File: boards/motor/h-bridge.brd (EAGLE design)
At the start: 44.5 x 44.5 mm, 11 parts

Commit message: text change for V_batt resistors
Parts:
- BATT_H: value (none) -> 715k
- BATT_L: value (none) -> 165k
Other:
- board text added: "WolfBot Motor Board v2013.08.08"
- board text removed: "WolfBot Motor Board v2013.07.08"
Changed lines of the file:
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@@
 <dimension x1="3.058334375" y1="39.149025" x2="5.196665625" y2="41.495975" x3="-10.160003125" y3="53.339996875" textsize="1.778" layer="47" dtype="diameter" unit="inch" precision="3"/>
 <text x="28.6512" y="16.4846" size="0.8128" layer="22" font="vector" rot="MR0">En</text>
-<text x="28.2575" y="28.8925" size="1.016" layer="22" font="vector" rot="MR0">M3+</text>
-<text x="28.2575" y="26.3525" size="1.016" layer="22" font="vector" rot="MR0">M3-</text>
+<text x="33.8201" y="30.2895" size="1.016" layer="22" font="vector" rot="MR0">M3+</text>
+<text x="33.8201" y="27.7495" size="1.016" layer="22" font="vector" rot="MR0">M3-</text>
 <text x="28.5496" y="14.6304" size="0.8128" layer="22" font="vector" rot="MR0">M1</text>
 <text x="28.6004" y="12.7" size="0.8128" layer="22" font="vector" rot="MR0">D1</text>
@@
 <text x="36.5125" y="9.8425" size="1.778" layer="21" font="vector">BAT</text>
 <text x="36.5125" y="29.845" size="1.778" layer="21" font="vector">OUT</text>
-<text x="28.2575" y="36.5125" size="1.016" layer="22" font="vector" rot="MR0">M1-</text>
-<text x="28.2575" y="33.9725" size="1.016" layer="22" font="vector" rot="MR0">M2+</text>
-<text x="28.2575" y="31.4325" size="1.016" layer="22" font="vector" rot="MR0">M2-</text>
-<text x="28.2575" y="39.0525" size="1.016" layer="22" font="vector" rot="MR0">M1+</text>
+<text x="33.8201" y="37.9095" size="1.016" layer="22" font="vector" rot="MR0">M1-</text>
+<text x="33.8201" y="35.3695" size="1.016" layer="22" font="vector" rot="MR0">M2+</text>
+<text x="33.8201" y="32.8295" size="1.016" layer="22" font="vector" rot="MR0">M2-</text>
+<text x="33.8201" y="40.4495" size="1.016" layer="22" font="vector" rot="MR0">M1+</text>
 <text x="14.7955" y="38.9255" size="1.27" layer="21" font="vector">H1</text>
 <text x="11.3665" y="1.0795" size="1.27" layer="21" font="vector">H2</text>
 <text x="43.942" y="1.9939" size="1.016" layer="21" font="vector" align="bottom-right">WolfBot
 Motor Board
-v2013.07.08</text>
+v2013.08.08</text>
 <text x="28.702" y="3.556" size="0.8128" layer="22" font="vector" rot="MR0">B_V</text>
 </plain>
@@
 <attribute name="VALUE" x="21.59" y="39.243" size="1.27" layer="27" ratio="10" rot="R270"/>
 </element>
-<element name="OUT" library="con-molex-micro-fit-3_0" package="43045-0206" value="" x="41.91" y="24.765" rot="R90"/>
+<element name="OUT" library="con-molex-micro-fit-3_0" package="43045-0206" value="" x="41.91" y="24.765" smashed="yes" rot="R90"/>
 <element name="H2" library="st-microelectronics" package="DIL16" value="L293D" x="19.685" y="10.795" smashed="yes" rot="R270">
 <attribute name="OC_NEWARK" value="56P8249" x="-15.875" y="-13.335" size="1.778" layer="27" rot="R270" display="off"/>
@@
 </element>
 <element name="MOTORS" library="SparkFun-Connectors" package="1X06_LOCK" value="" x="29.845" y="40.005" smashed="yes" rot="MR270">
-<attribute name="NAME" x="32.385" y="29.845" size="1.27" layer="26" font="vector" rot="MR90"/>
 <attribute name="VALUE" x="33.147" y="41.275" size="1.27" layer="28" font="vector" rot="MR270"/>
 </element>
@@
 <element name="U$1" library="wolfbot" package="WSP1-T2-M6" value="ESWITCH-WSP1" x="2.54" y="29.21"/>
 <element name="R1" library="resistor" package="R0603" value="" x="15.494" y="42.164" rot="MR180"/>
-<element name="BATT_H" library="resistor" package="R0603" value="" x="35.306" y="22.6568" rot="MR0"/>
-<element name="BATT_L" library="resistor" package="R0603" value="" x="27.686" y="1.905" rot="MR0"/>
-<element name="U$3" library="jst-ph" package="JST-PH-SMD-90*" value="JST-PH8-SMD-90" x="39.0144" y="20.3708" rot="MR270"/>
+<element name="BATT_H" library="resistor" package="R0603" value="715k" x="35.306" y="22.6568" smashed="yes" rot="MR0">
+<attribute name="VALUE" x="36.2712" y="23.9268" size="0.8128" layer="28" rot="MR0"/>
+</element>
+<element name="BATT_L" library="resistor" package="R0603" value="165k" x="27.686" y="1.905" smashed="yes" rot="MR0">
+<attribute name="VALUE" x="30.2006" y="2.7178" size="0.8128" layer="28" rot="MR270"/>
+</element>
+<element name="U$3" library="jst-ph" package="JST-PH-SMD-90*" value="JST-PH8-SMD-90" x="39.0144" y="20.3708" smashed="yes" rot="MR270">
+<attribute name="VALUE" x="39.0144" y="-2.4892" size="1.27" layer="28" rot="MR0"/>
+</element>
 </elements>
 <signals>
@@
 <vertex x="48.26" y="48.26"/>
 </polygon>
-<polygon width="0.508" layer="16">
+<polygon width="0.508" layer="16" spacing="0.8128">
 <vertex x="-2.54" y="45.72"/>
 <vertex x="-2.54" y="-2.54"/>

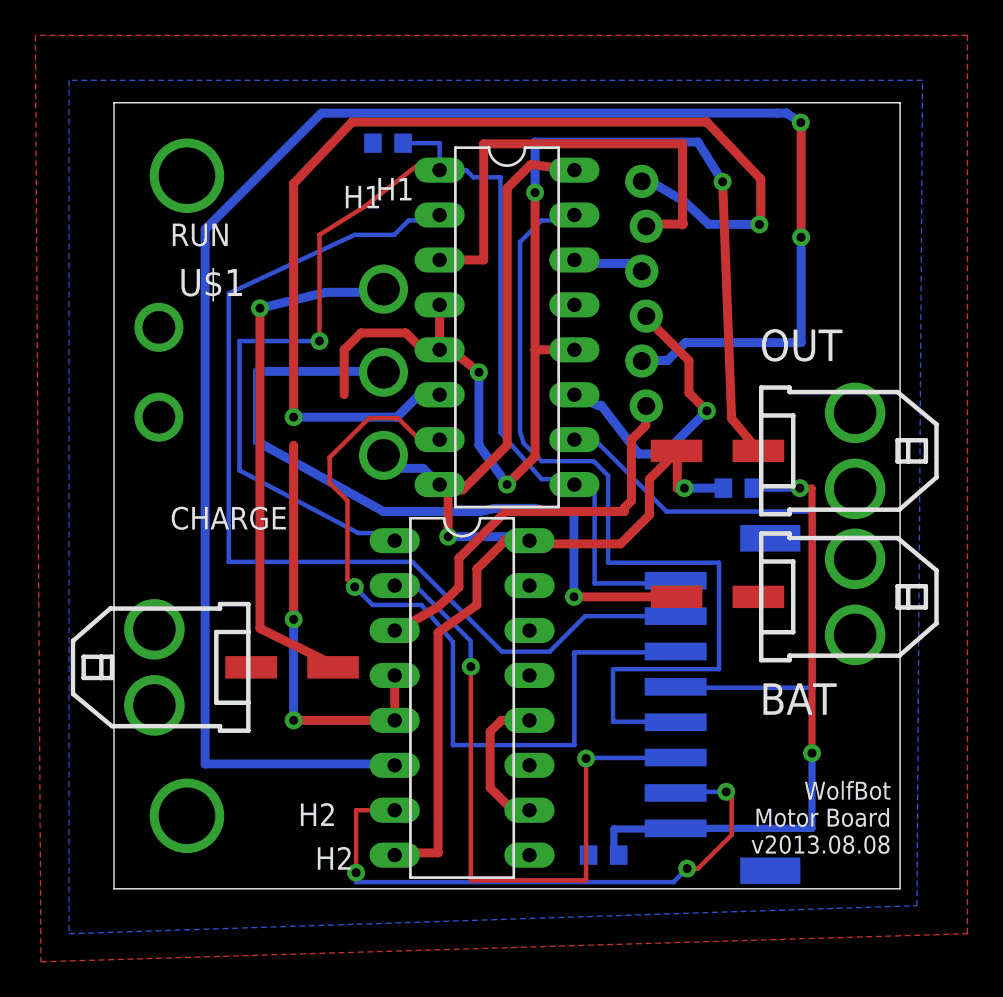
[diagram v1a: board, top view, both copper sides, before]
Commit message: Fix motor board silk screening
- add tValues and bValues to CAM job
- move resistor labels
- remove unwanted labels
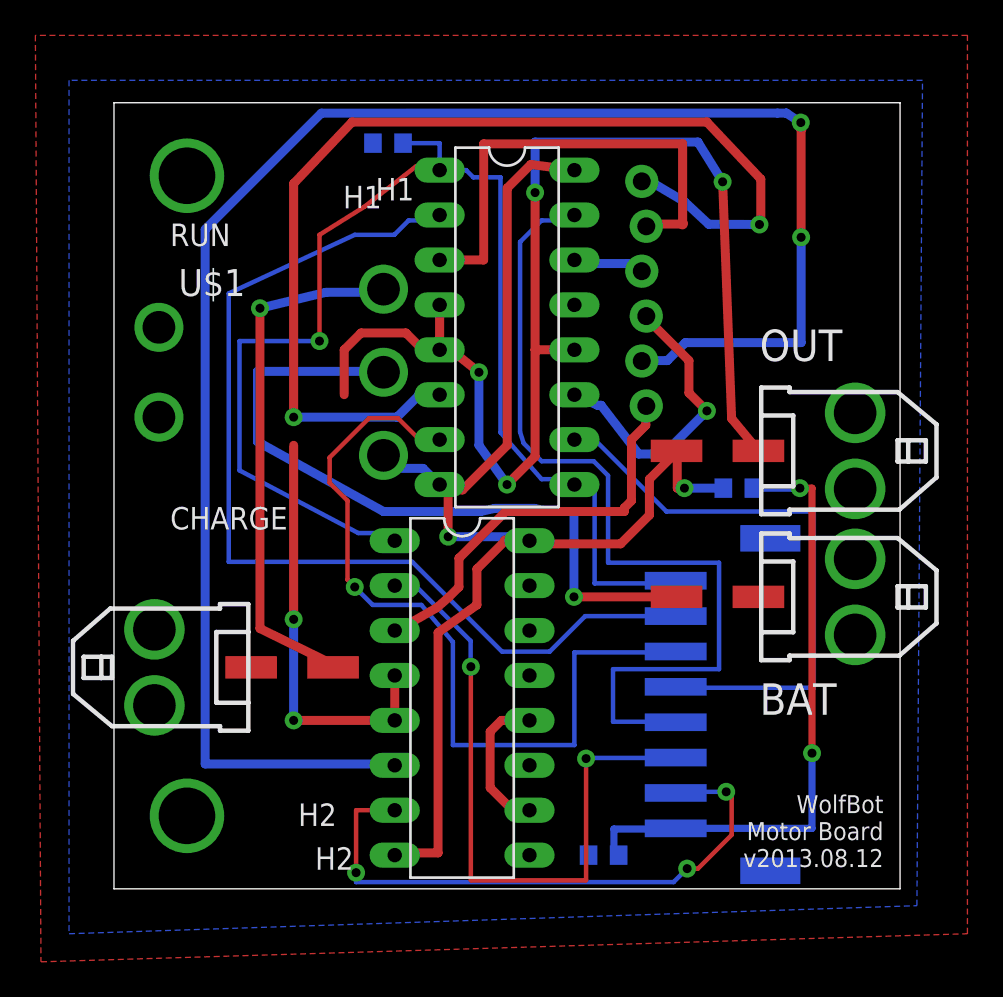
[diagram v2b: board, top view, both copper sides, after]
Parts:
- R1: value (none) -> 10k
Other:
- board text added: "WolfBot Motor Board v2013.08.12"
- board text removed: "WolfBot Motor Board v2013.08.08"
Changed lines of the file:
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@@
 <layer number="23" name="tOrigins" color="15" fill="1" visible="yes" active="yes"/>
 <layer number="24" name="bOrigins" color="15" fill="1" visible="yes" active="yes"/>
-<layer number="25" name="tNames" color="7" fill="1" visible="yes" active="yes"/>
-<layer number="26" name="bNames" color="7" fill="1" visible="yes" active="yes"/>
+<layer number="25" name="tNames" color="7" fill="1" visible="no" active="yes"/>
+<layer number="26" name="bNames" color="7" fill="1" visible="no" active="yes"/>
 <layer number="27" name="tValues" color="7" fill="1" visible="yes" active="yes"/>
 <layer number="28" name="bValues" color="7" fill="1" visible="yes" active="yes"/>
@@
 <text x="14.7955" y="38.9255" size="1.27" layer="21" font="vector">H1</text>
 <text x="11.3665" y="1.0795" size="1.27" layer="21" font="vector">H2</text>
-<text x="43.942" y="1.9939" size="1.016" layer="21" font="vector" align="bottom-right">WolfBot
+<text x="43.5102" y="1.2319" size="1.016" layer="21" font="vector" align="bottom-right">WolfBot
 Motor Board
-v2013.08.08</text>
+v2013.08.12</text>
 <text x="28.702" y="3.556" size="0.8128" layer="22" font="vector" rot="MR0">B_V</text>
 </plain>
@@
 <attribute name="OC_FARNELL" value="9589619" x="-0.635" y="7.62" size="1.778" layer="27" rot="R270" display="off"/>
 <attribute name="NAME" x="12.954" y="38.481" size="1.27" layer="25" ratio="10"/>
-<attribute name="VALUE" x="21.59" y="39.243" size="1.27" layer="27" ratio="10" rot="R270"/>
+<attribute name="VALUE" x="21.59" y="37.0078" size="1.27" layer="27" ratio="10" rot="R270"/>
 </element>
 <element name="OUT" library="con-molex-micro-fit-3_0" package="43045-0206" value="" x="41.91" y="24.765" smashed="yes" rot="R90"/>
@@
 <attribute name="OC_FARNELL" value="9589619" x="-15.875" y="-13.335" size="1.778" layer="27" rot="R270" display="off"/>
 <attribute name="NAME" x="10.414" y="3.556" size="1.27" layer="25" ratio="10"/>
-<attribute name="VALUE" x="19.05" y="18.288" size="1.27" layer="27" ratio="10" rot="R270"/>
+<attribute name="VALUE" x="19.05" y="9.0678" size="1.27" layer="27" ratio="10" rot="R270"/>
 </element>
 <element name="MOTORS" library="SparkFun-Connectors" package="1X06_LOCK" value="" x="29.845" y="40.005" smashed="yes" rot="MR270">
@@
 <element name="BAT" library="con-molex-micro-fit-3_0" package="43045-0206" value="" x="41.91" y="16.51" rot="R90"/>
 <element name="CHARGE" library="con-molex-micro-fit-3_0" package="43045-0206" value="" x="2.286" y="12.5222" rot="R270"/>
-<element name="U$1" library="wolfbot" package="WSP1-T2-M6" value="ESWITCH-WSP1" x="2.54" y="29.21"/>
-<element name="R1" library="resistor" package="R0603" value="" x="15.494" y="42.164" rot="MR180"/>
+<element name="U$1" library="wolfbot" package="WSP1-T2-M6" value="ESWITCH-WSP1" x="2.54" y="29.21" smashed="yes">
+<attribute name="NAME" x="3.65" y="33.52" size="1.524" layer="25" ratio="10"/>
+</element>
+<element name="R1" library="resistor" package="R0603" value="10k" x="15.494" y="42.164" smashed="yes" rot="MR180">
+<attribute name="VALUE" x="12.0904" y="42.4434" size="0.8128" layer="28" rot="MR180"/>
+</element>
 <element name="BATT_H" library="resistor" package="R0603" value="715k" x="35.306" y="22.6568" smashed="yes" rot="MR0">
 <attribute name="VALUE" x="36.2712" y="23.9268" size="0.8128" layer="28" rot="MR0"/>
 </element>
 <element name="BATT_L" library="resistor" package="R0603" value="165k" x="27.686" y="1.905" smashed="yes" rot="MR0">
-<attribute name="VALUE" x="30.2006" y="2.7178" size="0.8128" layer="28" rot="MR270"/>
-</element>
-<element name="U$3" library="jst-ph" package="JST-PH-SMD-90*" value="JST-PH8-SMD-90" x="39.0144" y="20.3708" smashed="yes" rot="MR270">
-<attribute name="VALUE" x="39.0144" y="-2.4892" size="1.27" layer="28" rot="MR0"/>
-</element>
+<attribute name="VALUE" x="26.035" y="3.5814" size="0.8128" layer="28" rot="MR270"/>
+</element>
+<element name="U$3" library="jst-ph" package="JST-PH-SMD-90*" value="JST-PH8-SMD-90" x="39.0144" y="20.3708" smashed="yes" rot="MR270"/>
 </elements>
 <signals>

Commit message: Fixed pull down, and three res sizes
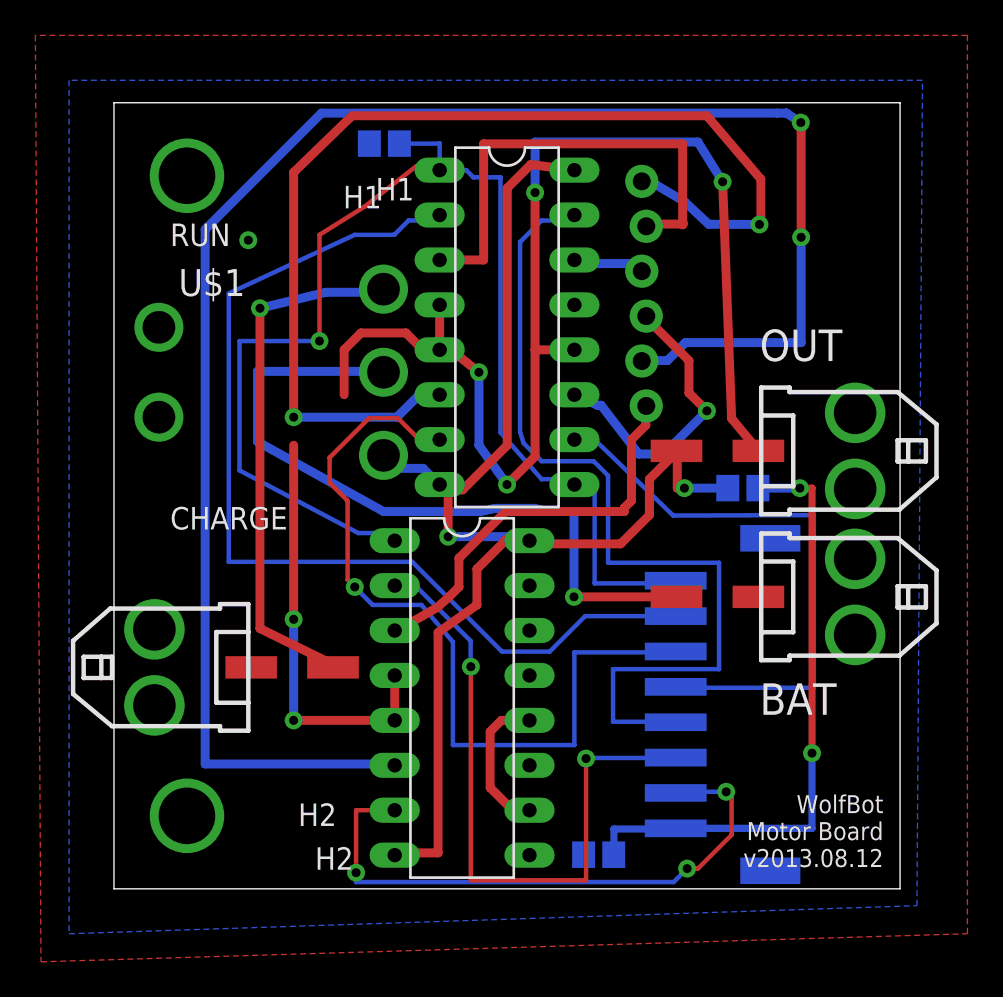
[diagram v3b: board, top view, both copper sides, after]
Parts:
- removed R1: 10k, resistor:R0603
- added EN_D: 10k, resistor:R0805
- BATT_H, BATT_L: device resistor:R0603 -> resistor:R0805
- moved BATT_L 0.28 mm to (27.4, 1.93), turned to 180 degrees
- moved BATT_H 0.25 mm to (35.6, 22.7)
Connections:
- net ENABLE: now also EN_D.2; no longer R1.2
- net GND: now also BATT_L.1, EN_D.1; no longer BATT_L.2, R1.1
- net N$2: now also BATT_L.2; no longer BATT_L.1
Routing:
- net M1+: track 61.4 -> 62.1 mm
- net M3_DIR: track 35.5 -> 36.1 mm
- net N$2: track 36.8 -> 36.3 mm
- net GND: vias 6 -> 7

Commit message: Cleanup issues, working on powerboard res move
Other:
- board text added: "WolfBot Motor Board v2013.09.26"
- board text removed: "WolfBot Motor Board v2013.08.12"
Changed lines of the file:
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@@
 <setting verticaltext="up"/>
 </settings>
-<grid distance="1" unitdist="mil" unit="mil" style="lines" multiple="10" display="yes" altdistance="0.0125" altunitdist="inch" altunit="inch"/>
+<grid distance="0.01" unitdist="mm" unit="mm" style="lines" multiple="10" display="yes" altdistance="0.0125" altunitdist="inch" altunit="inch"/>
 <layers>
 <layer number="1" name="Top" color="4" fill="1" visible="yes" active="yes"/>
@@
 <text x="43.5102" y="1.2319" size="1.016" layer="21" font="vector" align="bottom-right">WolfBot
 Motor Board
-v2013.08.12</text>
+v2013.09.26</text>
 <text x="28.702" y="3.556" size="0.8128" layer="22" font="vector" rot="MR0">B_V</text>
+<circle x="4.1275" y="40.3225" radius="3.668" width="0.4064" layer="21"/>
+<text x="4.495" y="36.3474" size="1.27" layer="22" font="vector" rot="MR0">RUN</text>
+<text x="3.175" y="20.32" size="1.27" layer="21" font="vector">CHARGE</text>
+<text x="7.735" y="20.26" size="1.27" layer="22" font="vector" rot="MR0">CHARGE</text>
+<circle x="4.1275" y="4.1275" radius="3.668" width="0.4064" layer="21"/>
 </plain>
 <attributes>

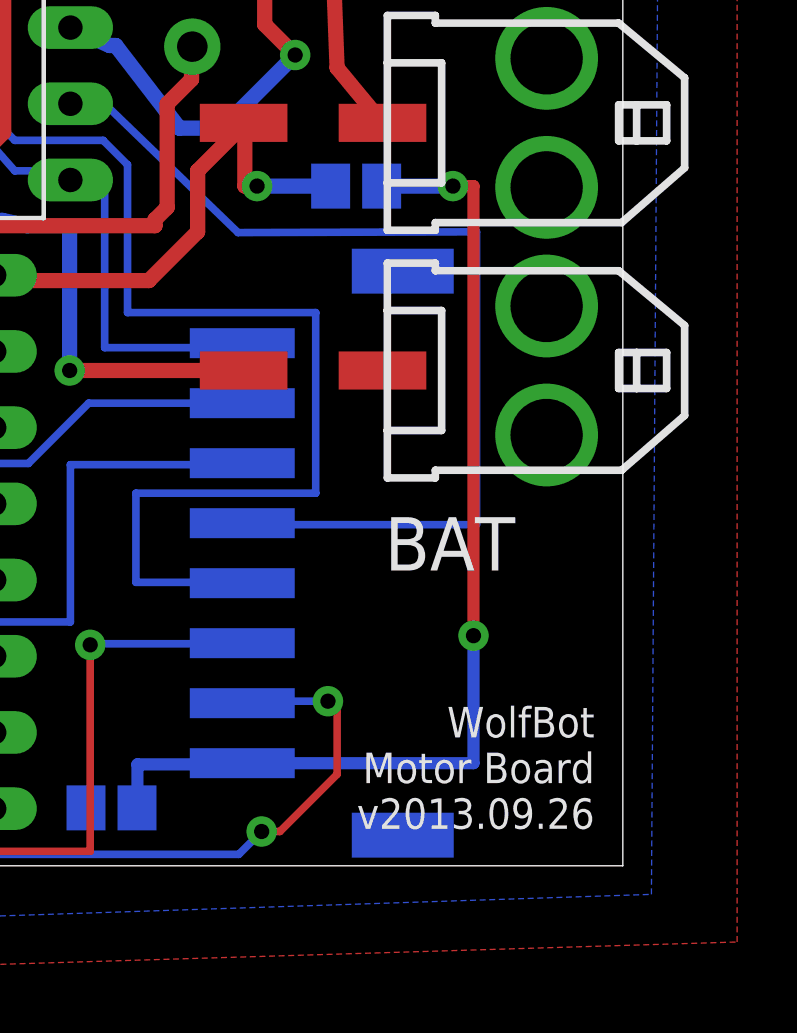
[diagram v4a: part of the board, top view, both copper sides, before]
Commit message: fixed via short problem
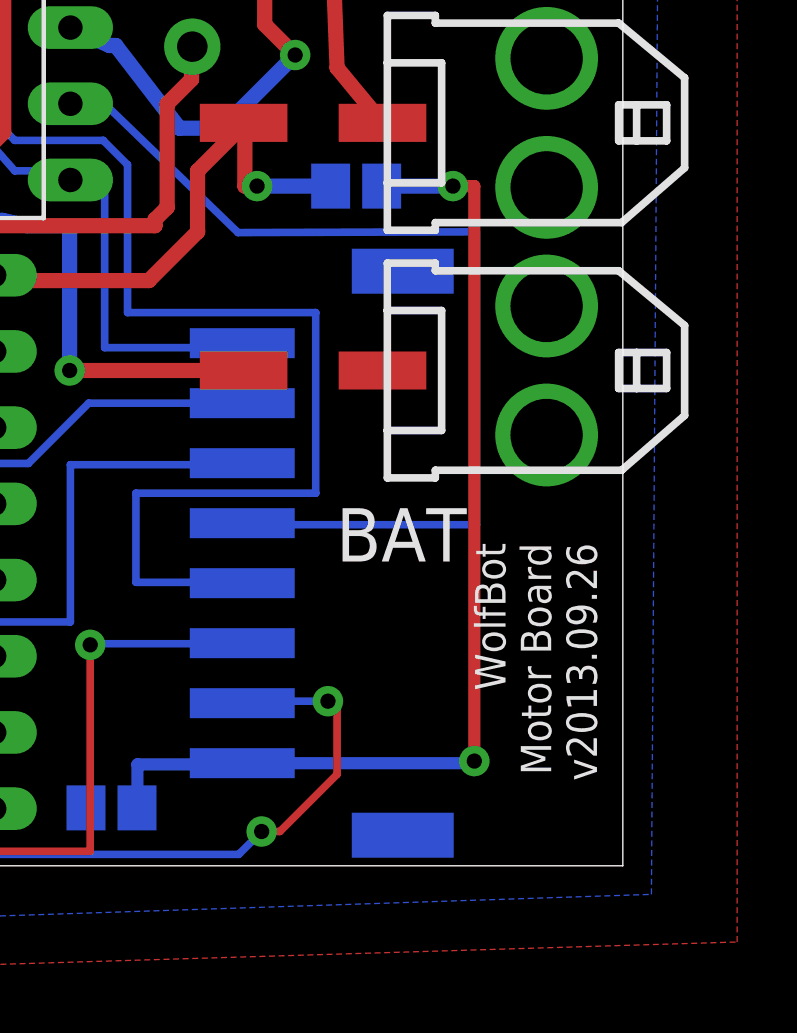
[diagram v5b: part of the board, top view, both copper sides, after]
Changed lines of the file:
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@@
 <text x="3.175" y="20.32" size="1.27" layer="21" font="vector">CHARGE</text>
 <text x="3.175" y="36.3474" size="1.27" layer="21" font="vector">RUN</text>
-<text x="36.5125" y="9.8425" size="1.778" layer="21" font="vector">BAT</text>
+<text x="34.8925" y="10.1425" size="1.778" layer="21" font="vector">BAT</text>
 <text x="36.5125" y="29.845" size="1.778" layer="21" font="vector">OUT</text>
 <text x="33.8201" y="37.9095" size="1.016" layer="22" font="vector" rot="MR0">M1-</text>
@@
 <text x="14.7955" y="38.9255" size="1.27" layer="21" font="vector">H1</text>
 <text x="11.3665" y="1.0795" size="1.27" layer="21" font="vector">H2</text>
-<text x="43.5102" y="1.2319" size="1.016" layer="21" font="vector" align="bottom-right">WolfBot
+<text x="43.5881" y="10.7602" size="1.016" layer="21" font="vector" rot="R90" align="bottom-right">WolfBot
 Motor Board
 v2013.09.26</text>
@@
 <wire x1="28.2702" y1="3.38125" x2="31.2535625" y2="3.38125" width="0.4064" layer="16"/>
 <via x="38.7858" y="22.6568" extent="1-16" drill="0.508" alwaysstop="yes"/>
-<wire x1="38.7858" y1="22.6568" x2="39.4716" y2="22.6568" width="0.4064" layer="1"/>
-<wire x1="39.4716" y1="22.6568" x2="39.4716" y2="7.6708" width="0.4064" layer="1"/>
-<via x="39.4716" y="7.6708" extent="1-16" drill="0.508" alwaysstop="yes"/>
-<wire x1="39.4716" y1="7.6708" x2="39.4716" y2="3.4208" width="0.4064" layer="16"/>
+<wire x1="38.7858" y1="22.6568" x2="39.5" y2="22.6568" width="0.4064" layer="1"/>
+<wire x1="39.5" y1="22.6568" x2="39.5" y2="3.4908" width="0.4064" layer="1"/>
+<via x="39.5" y="3.4908" extent="1-16" drill="0.508" alwaysstop="yes"/>
+<wire x1="39.5" y1="3.4908" x2="39.4716" y2="3.4208" width="0.4064" layer="16"/>
 <wire x1="39.4716" y1="3.4208" x2="31.7644" y2="3.4208" width="0.4064" layer="16"/>
 <contactref element="BATT_H" pad="1"/>
@@
 <wire x1="36.41" y1="22.6568" x2="38.7858" y2="22.6568" width="0.508" layer="16"/>
 </signal>
-<signal name="N$1">
+<signal name="N$116">
 <via x="4.1275" y="4.1275" extent="1-16" drill="3.2"/>
 <via x="4.1275" y="40.3225" extent="1-16" drill="3.2"/>
